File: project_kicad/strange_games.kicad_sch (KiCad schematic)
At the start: 130 parts, among them J1 Display, M1 Motor_DC, Q1 Si2302A, Q2 Q_Photo, Q3 Si2302A, Q4 Q_Photo, SW1 SW_Push, SW10 SW_Push, SW2 SW_Push, SW3 SW_Push, SW4 SW_Push, SW5 SW_Push, SW6 SW_Push, SW7 SW_Push, SW8 SW_Push, SW9 SW_Push, U1 charge controller, U2 boost converter, U3 LDL1117S33R, U4 ESP32-DEVKIT-V1, U5 TMP112xxDRL, U6 vibrating_sensor, U7 LSM6DS3, U8 MQ-135 gas sensor

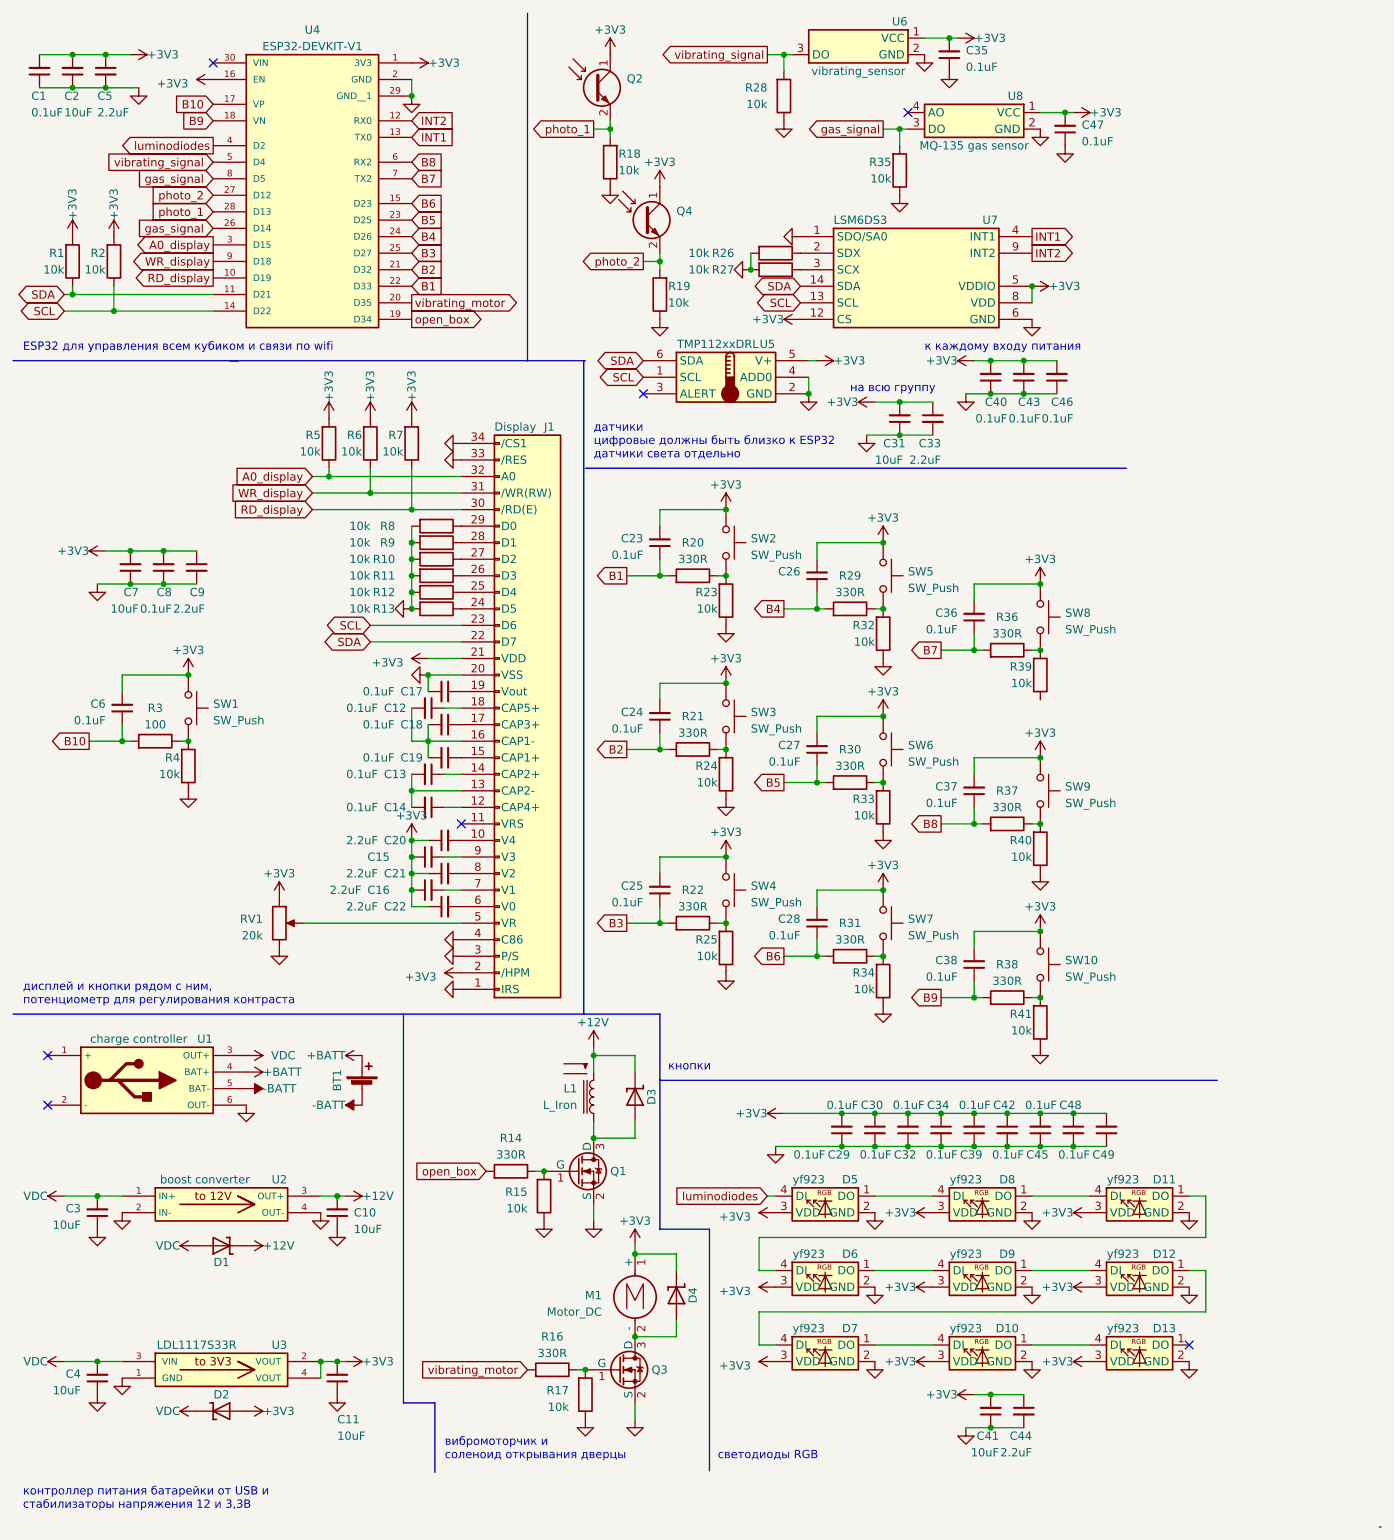
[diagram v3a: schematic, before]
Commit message: remastered display pins in the kicad scheme
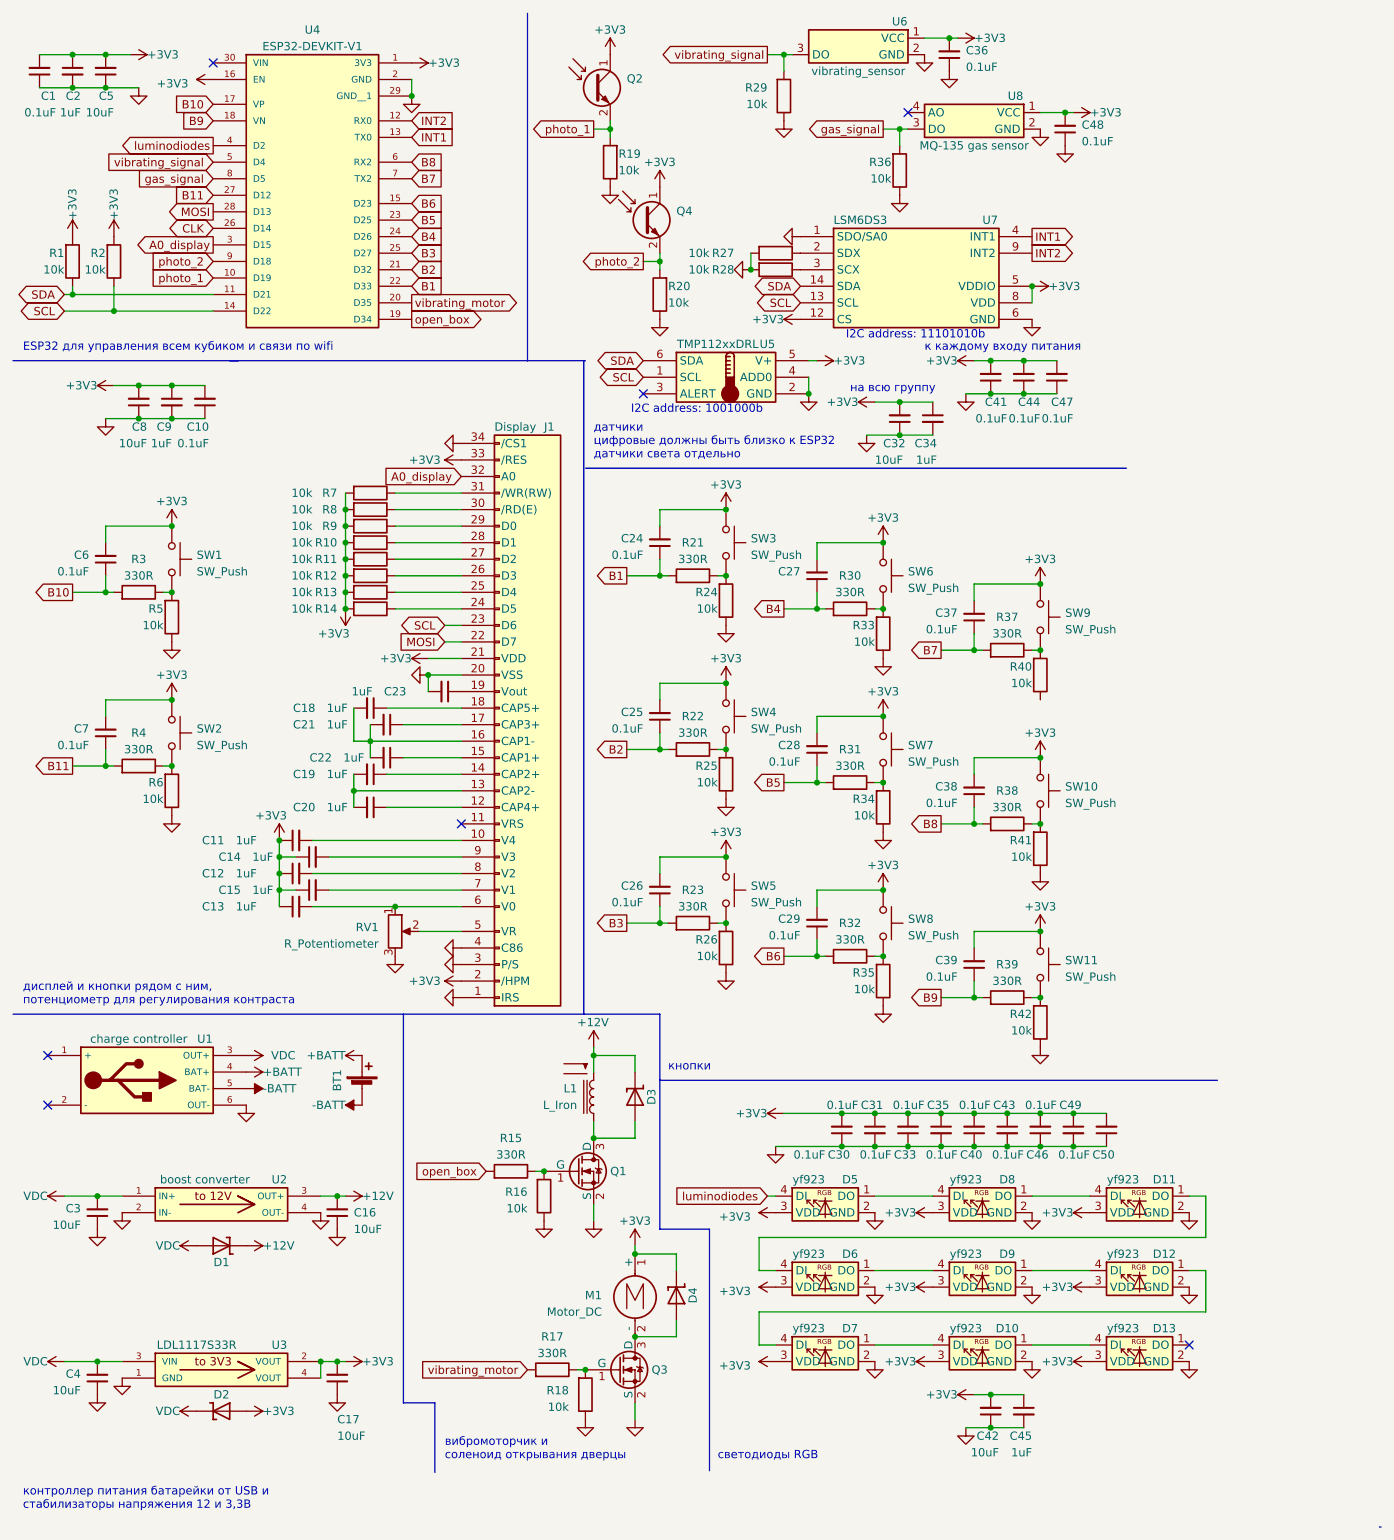
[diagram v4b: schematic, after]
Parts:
- removed C16, C17, C20, C33, C44, C5: C_Generic, PCM_Capacitor_SMD_AKL:C_0402_1005Metric, symbol Library:C_Generic
- removed R5: 10k_0805, PCM_4ms_Resistor:R_0805_2012Metric, symbol Library:1.2k_0603
- added C11, C14, C2, C23, C34, C45, C7: C_Generic, PCM_Capacitor_SMD_AKL:C_0402_1005Metric, symbol Library:C_Generic
- added R4: 330_0805, PCM_4ms_Resistor:R_0805_2012Metric, symbol Library:1.2k_0603
- added R8: 10k_0805, PCM_4ms_Resistor:R_0805_2012Metric, symbol Library:1.2k_0603
- added SW2: SW_Push, Button_Switch_THT:SW_PUSH-12mm, symbol Switch:SW_Push
- C12, C13, C18, C19: Capacity 0.1uF -> 1uF; Voltage 10V -> 16V
- C15, C21, C22, C9: Capacity 2.2uF -> 1uF; Display ?F -> (none); Voltage 6.3V -> 16V
- C20: renamed from C14; Capacity 0.1uF -> 1uF; Voltage 10V -> 16V
- R3: value 100_0805 -> 330_0805; Display 100 -> 330R; Specifications 100, 1%, 1/10W, 0805 -> 330, 1%, 1/10W, 0805
- RV1: value TRIM -> R_Potentiometer; footprint SnapEDA Library:TRIM_3362P-1-203LF -> (none); Сопротивление 20k -> (none)
- renumbered C8 to C10, C10 to C16, C11 to C17, C23 to C24, C24 to C25, C25 to C26, C26 to C27, C27 to C28, C28 to C29, C29 to C30, C30 to C31, C31 to C32, C32 to C33, C34 to C35, C35 to C36, C36 to C37, C37 to C38, C38 to C39, C39 to C40, C40 to C41, C41 to C42, C42 to C43, C43 to C44, C45 to C46, C46 to C47, C47 to C48, C48 to C49, C2 to C5, C49 to C50, C7 to C8, R9 to R10, R10 to R11, R11 to R12, R12 to R13, R13 to R14, R14 to R15, R15 to R16, R16 to R17, R17 to R18, R18 to R19, R19 to R20, R20 to R21, R21 to R22, R22 to R23, R23 to R24, R24 to R25, R25 to R26, R26 to R27, R27 to R28, R28 to R29, R29 to R30, R30 to R31, R31 to R32, R32 to R33, R33 to R34, R34 to R35, R35 to R36, R36 to R37, R37 to R38, R38 to R39, R39 to R40, R40 to R41, R41 to R42, R4 to R5, R8 to R9, SW9 to SW10, SW10 to SW11, SW2 to SW3, SW3 to SW4, SW4 to SW5, SW5 to SW6, SW6 to SW7, SW7 to SW8, SW8 to SW9
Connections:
- net +3V3: now also C12.1, C13.1, J1.33 (/RES), R10.2, R11.2, R12.2, R13.2, R14.2, R9.2, C11.1, C14.1, C2.1, C34.1, C45.1, C7.2, R8.2, SW2.1; no longer C21.1, C22.1, R6.2, RV1.1
- net GND: now also R6.1, C2.2, C23.2, C34.2, C45.2; no longer J1.33 (/RES), R10.2, R11.2, R12.2, R13.2, R14.2, R9.2
- net SDA: no longer J1.22 (D7)
- net gas_signal: no longer U4.26 (D14)
- net photo_1: now also U4.10 (D19); no longer U4.28 (D13)
- net photo_2: now also U4.9 (D18); no longer U4.27 (D12)
- net at J1.19 (Vout): now also C23.1
- net at J1.14 (CAP2+): now also C19.1; no longer C13.1
- net at C20.2, J1.13 (CAP2-): now also C19.2; no longer C13.2
- net at C18.1: now also J1.18 (CAP5+); no longer J1.17 (CAP3+)
- net at C18.2, J1.16 (CAP1-): now also C21.2, C22.2; no longer C12.2, C19.2
- net at J1.10 (V4): now also C11.2
- net at J1.15 (CAP1+): now also C22.1; no longer C19.1
- net at J1.7 (V1): now also C15.2
- net at J1.8 (V2): now also C12.2; no longer C21.2
- net at J1.9 (V3): now also C14.2; no longer C15.2
- net at J1.6 (V0): now also C13.2, RV1.1; no longer C22.2
- removed net RD_display: J1.30 (/RD(E)), R7.1, U4.10 (D19)
- removed net WR_display: J1.31 (/WR(RW)), R6.1, U4.9 (D18)
- new net: J1.30 (/RD(E)), R8.1
- new net: J1.31 (/WR(RW)), R7.1
- new net: C21.1, J1.17 (CAP3+)
- new net: R4.1, R6.2, SW2.2
- new net B11: C7.1, R4.2, U4.27 (D12)
- new net CLK: U4.26 (D14)
- new net MOSI: J1.22 (D7), U4.28 (D13)
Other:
- note added: "I2C address: 1001000b"
- note added: "I2C address: 11101010b"
- moved on the sheet: C10, C20, C5, C6, C8, J1, R10, R11, R12, R13, R14, R5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

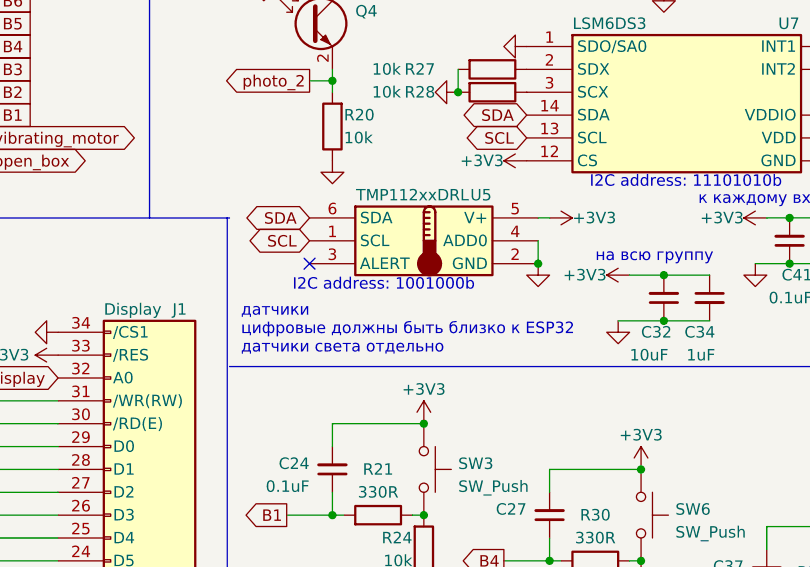
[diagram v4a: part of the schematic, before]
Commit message: made data class
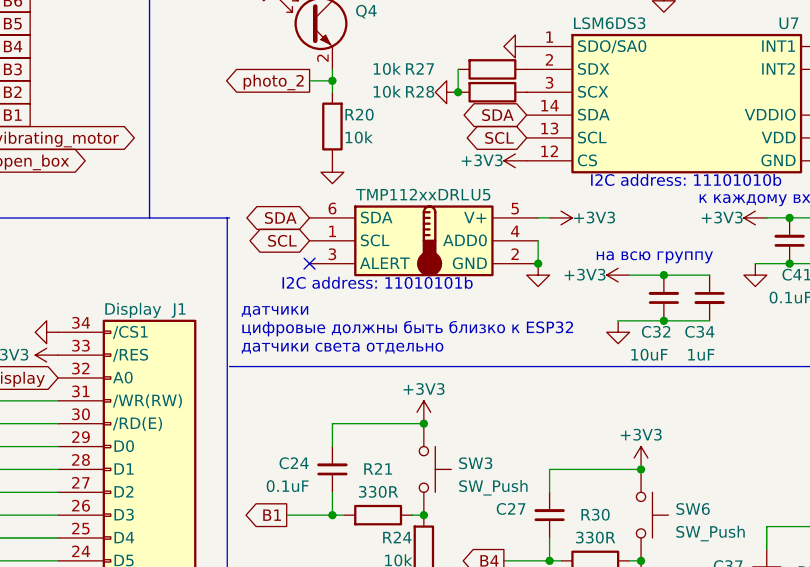
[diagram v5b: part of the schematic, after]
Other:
- note added: "I2C address: 11010101b"
- note removed: "I2C address: 1001000b"
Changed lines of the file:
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@@
     (effects (font (size 1.27 1.27)) (justify left bottom))
   )
-  (text "I2C address: 1001000b" (at 114.935 66.675 0)
+  (text "I2C address: 11010101b" (at 113.665 66.675 0)
     (effects (font (size 1.27 1.27)) (justify left bottom))
   )

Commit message: pcb updates
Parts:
- removed C8: C_Generic, PCM_Capacitor_SMD_AKL:C_0805_2012Metric, symbol Library:C_Generic
- removed C9: C_Generic, PCM_Capacitor_SMD_AKL:C_0402_1005Metric, symbol Library:C_Generic
- C2: footprint PCM_Capacitor_SMD_AKL:C_0402_1005Metric -> PCM_Capacitor_SMD_AKL:C_0805_2012Metric; Capacity 1uF -> 10uF; Voltage 16V -> 6.3V
- C42: footprint PCM_Capacitor_SMD_AKL:C_0805_2012Metric -> PCM_Capacitor_SMD_AKL:C_0402_1005Metric; Capacity 10uF -> 0.1uF; Voltage 6.3V -> 16V
- C45: Capacity 1uF -> 0.1uF
- R27, R28: value 10k_0805 -> 330_0805; Display 10k -> 330R; Specifications 10K, 1%, 1/10W, 0805 -> 330, 1%, 1/10W, 0805
- RV1: footprint (none) -> SnapEDA Library:TRIM_3362P-1-203LF
- renumbered C27 to C25, C37 to C26, C25 to C27, C38 to C29, C26 to C37, C29 to C38, D12 to D10, D7 to D11, D10 to D12, D8 to D6, D11 to D7, D6 to D8, R24 to R22, R30 to R23, R33 to R24, R37 to R25, R40 to R26, R22 to R30, R25 to R31, R31 to R32, R34 to R33, R38 to R34, R41 to R35, R23 to R37, R26 to R38, R32 to R39, R35 to R40, R39 to R41, SW8 to SW10, SW6 to SW4, SW9 to SW5, SW4 to SW6, SW10 to SW8, SW5 to SW9
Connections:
- net +3V3: now also C42.1, U7.10 (NC), U7.11 (NC); no longer C2.1, C42.2, C5.2
- net B2: now also C25.1, R23.2; no longer C27.1, R30.2
- net B3: now also C26.1, R25.2; no longer C37.1, R37.2
- net B4: now also C27.1, R30.2; no longer C25.1, R23.2
- net B6: now also C29.1, R34.2, U4.13 (TX0); no longer C38.1, R39.2, U4.15 (D23)
- net B7: now also C37.1, R37.2; no longer C26.1, R25.2
- net B8: now also C38.1, R39.2; no longer C29.1, R34.2
- net GND: now also C2.1, C42.2, R26.1, U7.2 (SDX), U7.3 (SCX); no longer C2.2, C42.1, R27.2, R28.2
- net INT1: now also U4.10 (D19); no longer U4.13 (TX0)
- net INT2: now also U4.15 (D23); no longer U4.12 (RX0)
- net photo_1: now also R27.2, U4.12 (RX0); no longer U4.10 (D19)
- net photo_2: now also R28.2
- net at R27.1: now also C5.2; no longer U7.2 (SDX)
- net at R28.1: now also C2.2; no longer U7.3 (SCX)
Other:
- moved on the sheet: C10, Q2, Q4, R19, R20, U7
